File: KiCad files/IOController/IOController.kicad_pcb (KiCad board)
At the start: 2 copper layers, 22.5 x 48.5 mm, 13 parts, among them J1 AVR-ISP-6, J2 XT60 Horizontal Male, J3 XT60 Horizontal Socket, J4 Conn_01x02, J5 Conn_01x02, SW1 RotaryEncoder_Switch, SW2 SW_Push, U1 ATtiny85-20P, U3 LP2985-1.8

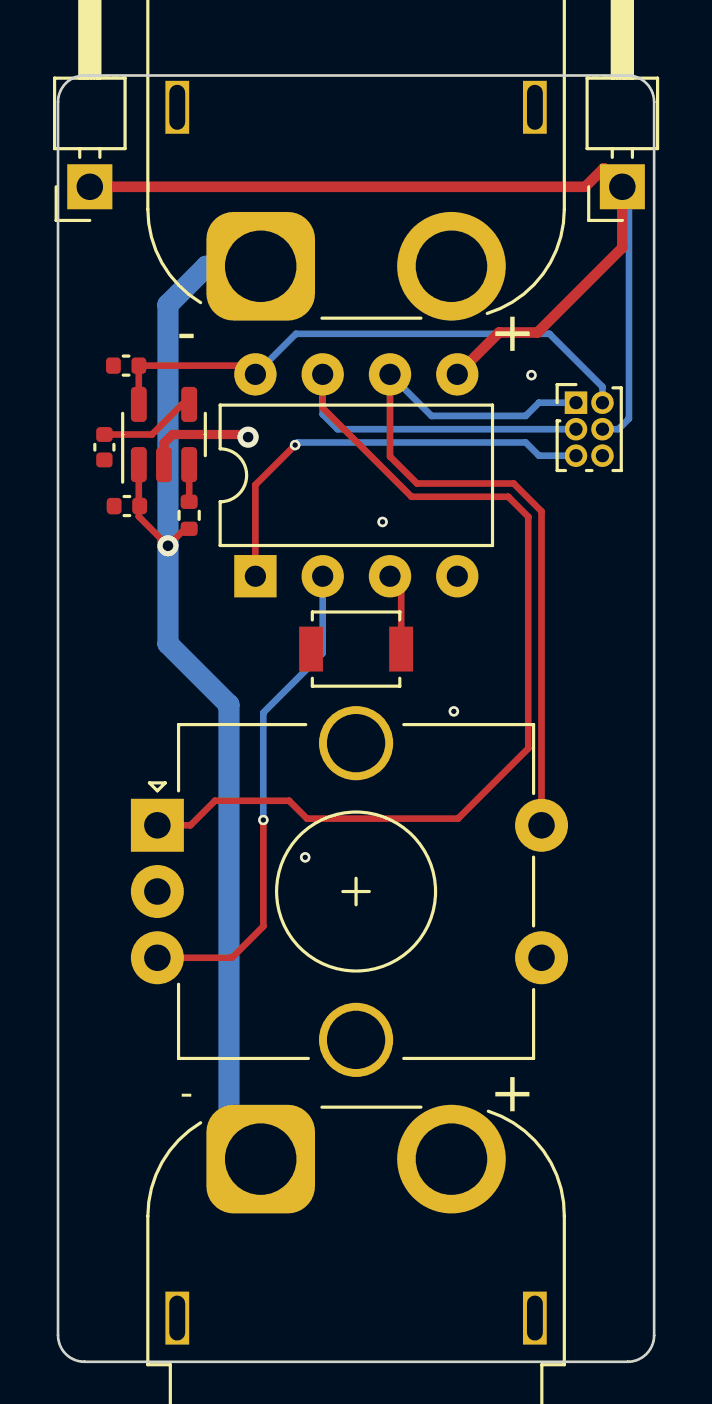
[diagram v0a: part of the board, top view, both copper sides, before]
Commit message: corrected VCC and GND being swapped
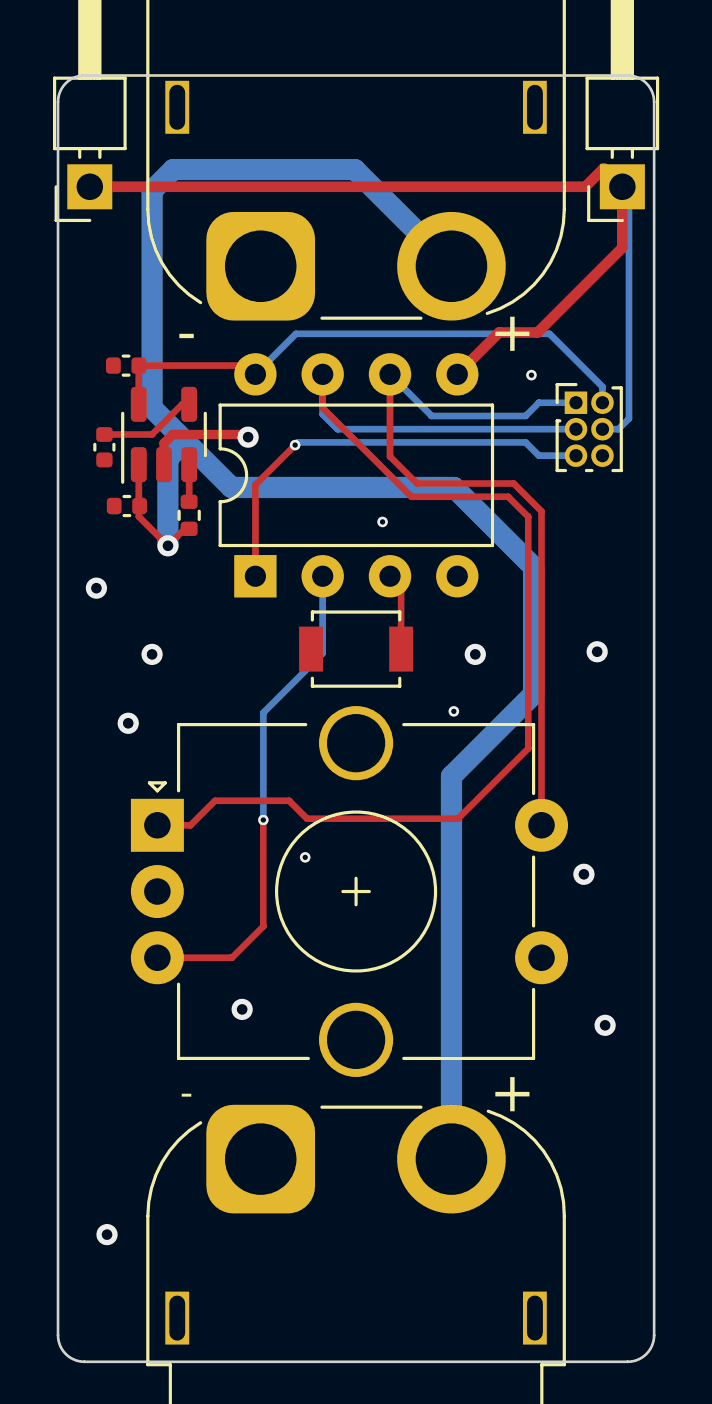
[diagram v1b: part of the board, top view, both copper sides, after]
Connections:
- J2 pad 1: VCC -> GND
- J2 pad 2: GND -> VCC
- J3 pad 1: VCC -> GND
- J3 pad 2: GND -> VCC
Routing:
- net VCC: track 42.4 -> 70.7 mm
- net GND: vias 5 -> 14
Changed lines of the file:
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@@
     (pad "" thru_hole rect locked (at 3.15 -6 180) (size 0.9 2) (drill oval 0.6 1.7) (layers "*.Cu" "*.Mask"))
     (pad "1" thru_hole roundrect locked (at 0 0 180) (size 4.1 4.1) (drill 2.7) (layers "*.Cu" "*.Mask") (roundrect_rratio 0.25)
-      (net 1 "VCC") (pinfunction "Pin_1") (pintype "passive"))
+      (net 2 "GND") (pinfunction "Pin_1") (pintype "passive"))
     (pad "2" thru_hole circle locked (at -7.2 0 180) (size 4.1 4.1) (drill 2.7) (layers "*.Cu" "*.Mask")
-      (net 2 "GND") (pinfunction "Pin_2") (pintype "passive"))
+      (net 1 "VCC") (pinfunction "Pin_2") (pintype "passive"))
     (model "${KIPRJMOD}/libraries/XT60PW FEMALE.STEP"
       (offset (xyz -3.6 15.15 4.5))
@@
     (pad "" thru_hole rect locked (at 10.35 -6) (size 0.9 2) (drill oval 0.6 1.7) (layers "*.Cu" "*.Mask"))
     (pad "1" thru_hole roundrect locked (at 0 0) (size 4.1 4.1) (drill 2.7) (layers "*.Cu" "*.Mask") (roundrect_rratio 0.25)
-      (net 1 "VCC") (pinfunction "Pin_1") (pintype "passive"))
+      (net 2 "GND") (pinfunction "Pin_1") (pintype "passive"))
     (pad "2" thru_hole circle locked (at 7.2 0) (size 4.1 4.1) (drill 2.7) (layers "*.Cu" "*.Mask")
-      (net 2 "GND") (pinfunction "Pin_2") (pintype "passive"))
+      (net 1 "VCC") (pinfunction "Pin_2") (pintype "passive"))
     (model "${KICAD6_3DMODEL_DIR}/Connector_AMASS.3dshapes/AMASS_XT60PW-M_1x02_P7.20mm_Horizontal.wrl"
       (offset (xyz 0 0 0))
@@
   (segment (start 24.3 49.1) (end 24.3 47.1375) (width 0.25) (layer "F.Cu") (net 1))
   (via (at 25.4 50.2) (size 0.8) (drill 0.4) (layers "F.Cu" "B.Cu") (net 1))
-  (segment (start 26.85 39.65) (end 25.4 41.1) (width 0.8) (layer "B.Cu") (net 1))
-  (segment (start 27.7 56.2) (end 27.7 72.15) (width 0.8) (layer "B.Cu") (net 1))
-  (segment (start 25.4 41.1) (end 25.4 53.9) (width 0.8) (layer "B.Cu") (net 1))
-  (segment (start 28.9 39.65) (end 26.85 39.65) (width 0.8) (layer "B.Cu") (net 1))
-  (segment (start 25.4 53.9) (end 27.7 56.2) (width 0.8) (layer "B.Cu") (net 1))
-  (segment (start 27.7 72.15) (end 28.9 73.35) (width 0.8) (layer "B.Cu") (net 1))
+  (segment (start 36.1 58.9) (end 39.2 55.8) (width 0.8) (layer "B.Cu") (net 1))
+  (segment (start 27.8 48) (end 26.05 46.25) (width 0.8) (layer "B.Cu") (net 1))
+  (segment (start 25.6 36) (end 32.45 36) (width 0.8) (layer "B.Cu") (net 1))
+  (segment (start 25.4 46.9) (end 26.05 46.25) (width 0.8) (layer "B.Cu") (net 1))
+  (segment (start 36.1 73.35) (end 36.1 58.9) (width 0.8) (layer "B.Cu") (net 1))
+  (segment (start 24.8 45) (end 24.8 36.8) (width 0.8) (layer "B.Cu") (net 1))
+  (segment (start 39.2 51) (end 36.2 48) (width 0.8) (layer "B.Cu") (net 1))
+  (segment (start 39.2 55.8) (end 39.2 51) (width 0.8) (layer "B.Cu") (net 1))
+  (segment (start 25.4 50.2) (end 25.4 46.9) (width 0.8) (layer "B.Cu") (net 1))
+  (segment (start 24.8 36.8) (end 25.6 36) (width 0.8) (layer "B.Cu") (net 1))
+  (segment (start 26.05 46.25) (end 24.8 45) (width 0.8) (layer "B.Cu") (net 1))
+  (segment (start 36.2 48) (end 27.8 48) (width 0.8) (layer "B.Cu") (net 1))
+  (segment (start 32.45 36) (end 36.1 39.65) (width 0.8) (layer "B.Cu") (net 1))
   (segment (start 28.325 46) (end 28.425 46.1) (width 0.35) (layer "F.Cu") (net 2))
   (segment (start 25.25 47.1375) (end 25.25 46.325) (width 0.35) (layer "F.Cu") (net 2))
   (segment (start 25.25 46.325) (end 25.575 46) (width 0.35) (layer "F.Cu") (net 2))
   (segment (start 25.575 46) (end 28.325 46) (width 0.35) (layer "F.Cu") (net 2))
+  (via (at 23.1 76.2) (size 0.8) (drill 0.4) (layers "F.Cu" "B.Cu") (free) (net 2))
   (via (at 28.425 46.1) (size 0.8) (drill 0.4) (layers "F.Cu" "B.Cu") (net 2))
+  (via (at 22.7 51.8) (size 0.8) (drill 0.4) (layers "F.Cu" "B.Cu") (free) (net 2))
   (via (at 39.12 43.76) (size 0.4) (drill 0.2) (layers "F.Cu" "B.Cu") (free) (net 2))
+  (via (at 41.9 68.3) (size 0.8) (drill 0.4) (layers "F.Cu" "B.Cu") (free) (net 2))
+  (via (at 37 54.3) (size 0.8) (drill 0.4) (layers "F.Cu" "B.Cu") (free) (net 2))
+  (via (at 24.8 54.3) (size 0.8) (drill 0.4) (layers "F.Cu" "B.Cu") (free) (net 2))
+  (via (at 23.9 56.9) (size 0.8) (drill 0.4) (layers "F.Cu" "B.Cu") (free) (net 2))
+  (via (at 28.2 67.7) (size 0.8) (drill 0.4) (layers "F.Cu" "B.Cu") (free) (net 2))
   (via (at 30.58 61.96) (size 0.4) (drill 0.2) (layers "F.Cu" "B.Cu") (free) (net 2))
   (via (at 36.19 56.45) (size 0.4) (drill 0.2) (layers "F.Cu" "B.Cu") (free) (net 2))
+  (via (at 41.1 62.6) (size 0.8) (drill 0.4) (layers "F.Cu" "B.Cu") (free) (net 2))
+  (via (at 41.6 54.2) (size 0.8) (drill 0.4) (layers "F.Cu" "B.Cu") (free) (net 2))
   (via (at 33.5 49.3) (size 0.4) (drill 0.2) (layers "F.Cu" "B.Cu") (net 2))
   (segment (start 30.65 60.5) (end 36.35 60.5) (width 0.25) (layer "F.Cu") (net 3))

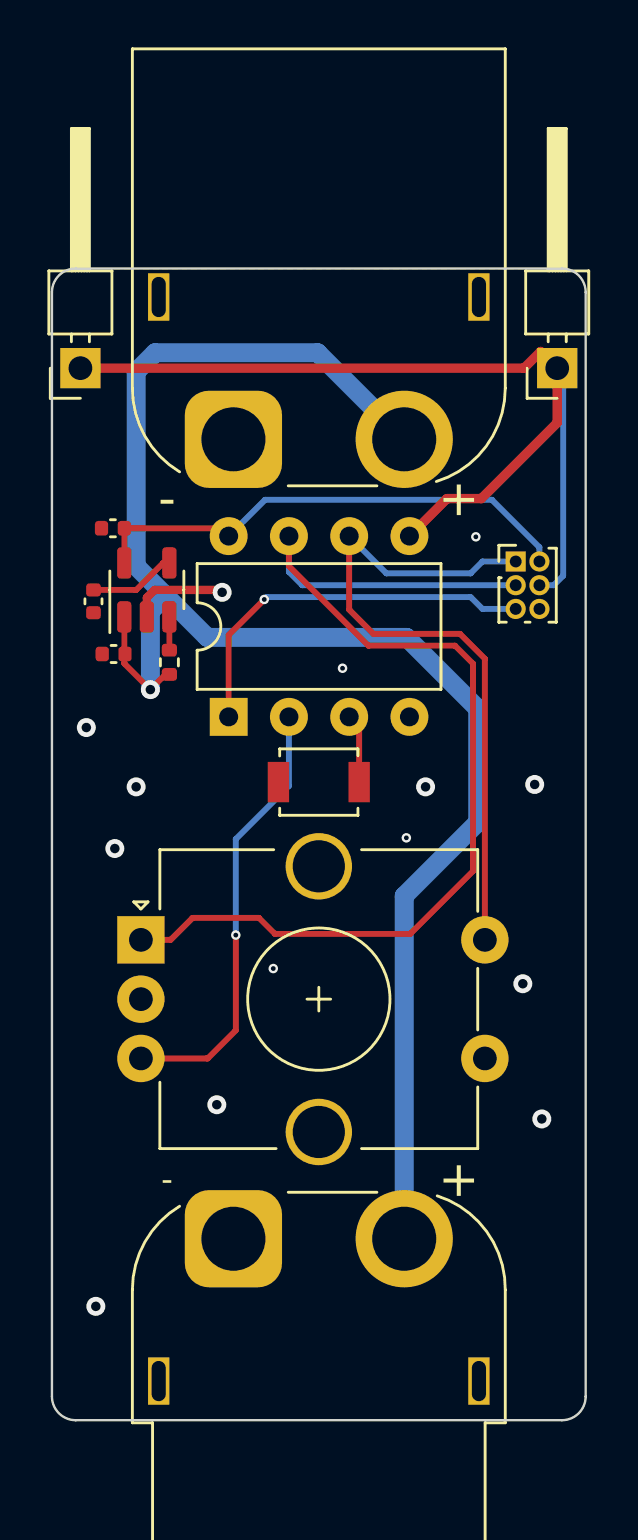
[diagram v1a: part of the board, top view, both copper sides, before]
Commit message: changed an XT60 to edge connector because I didnt like the XT60 and pin header setup.
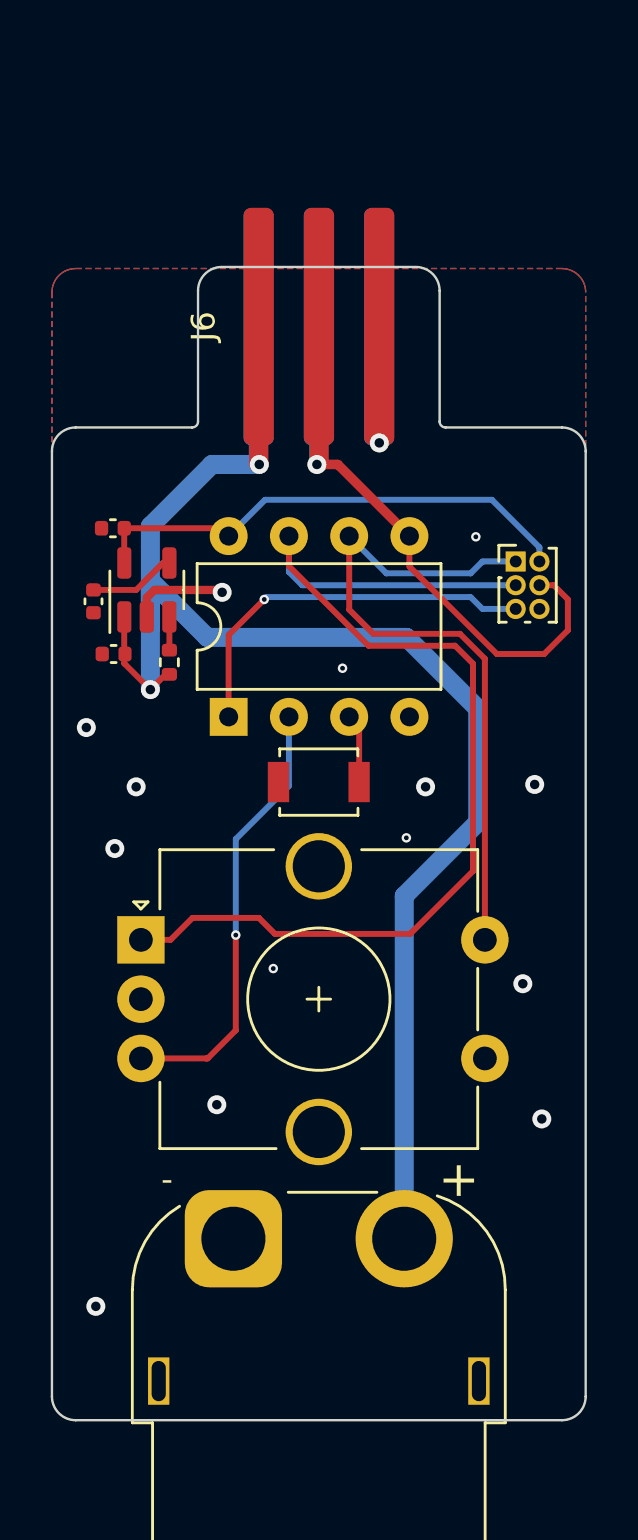
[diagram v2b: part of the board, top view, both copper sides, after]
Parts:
- removed J2: XT60 Horizontal Male, Connector_AMASS:AMASS_XT60PW-M_1x02_P7.20mm_Horizontal
- removed J4, J5: Conn_01x02, Connector_PinHeader_2.54mm:PinHeader_1x01_P2.54mm_Horizontal
- added J6: XT60 Horizontal Socket, Connector_PinHeader_2.54mm:PinHeader_1x03_P2.54mm_Vertical, F.Cu at (30.0, 34.9)
- added J6: XT60 Horizontal Socket, Connector_PinHeader_2.54mm:PinHeader_1x03_P2.54mm_Vertical, B.Cu at (30.0, 34.9)
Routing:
- net NPN-Gate: track 41.2 -> 29.5 mm, vias 0 -> 1
- net GND: track 4.16 -> 14.0 mm, vias 14 -> 15
- net VCC: track 70.7 -> 70.5 mm, vias 1 -> 2
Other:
- board size 22.5 x 48.5 mm -> 22.5 x 48.6 mm

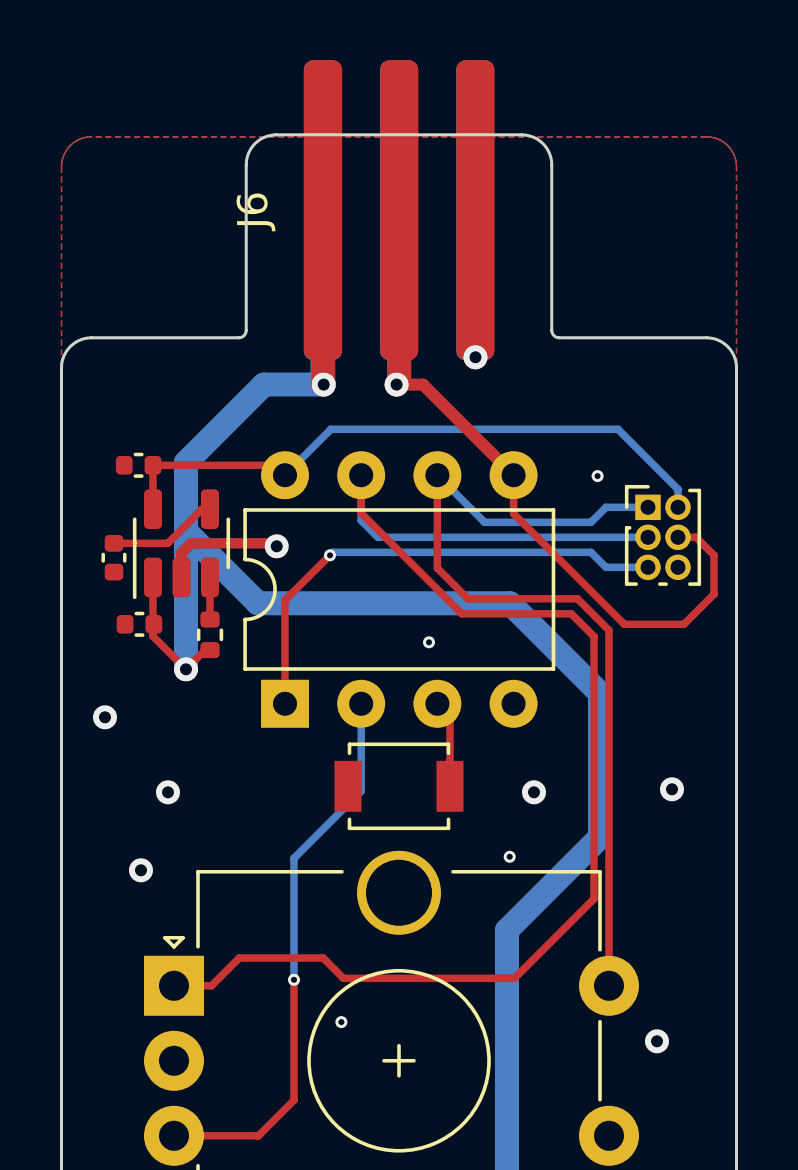
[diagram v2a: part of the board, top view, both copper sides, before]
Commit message: added footprints for some discontinued LEDs i have spare of, added level shifter to ensure gate voltage is above threshold
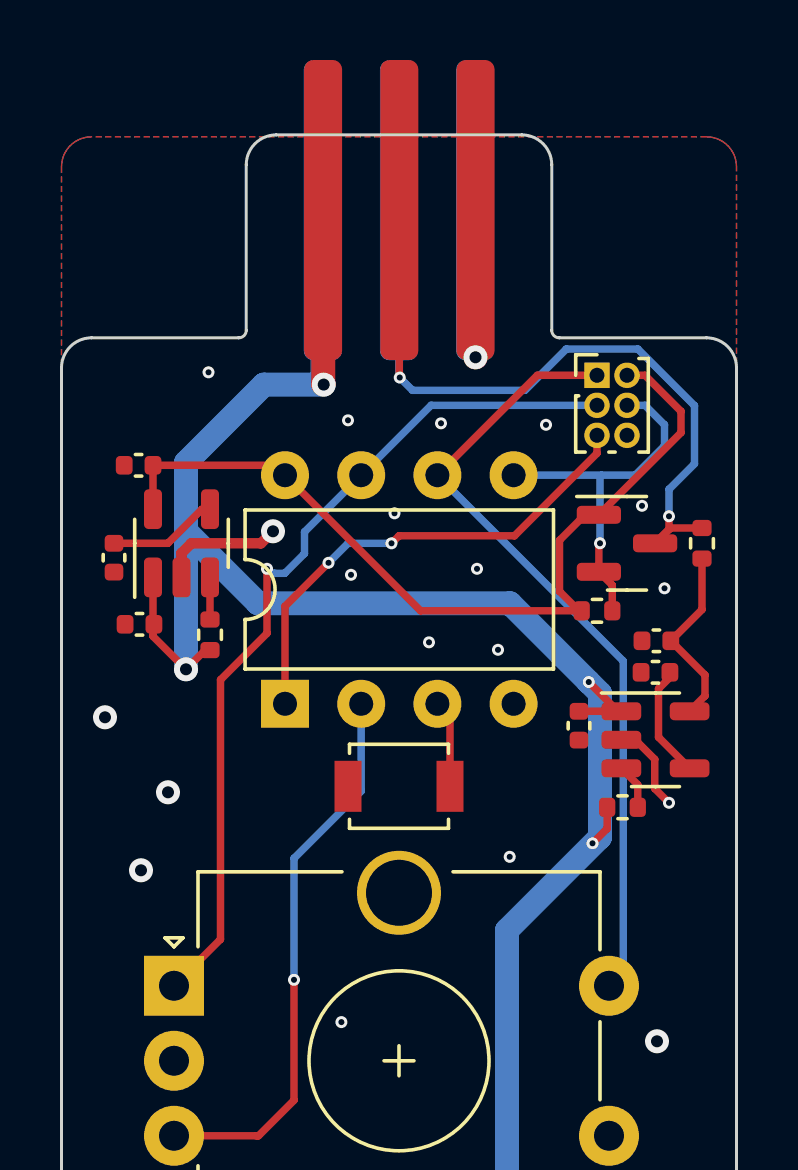
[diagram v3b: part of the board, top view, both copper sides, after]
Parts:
- added C4: 0402 1uF, Capacitor_SMD:C_0402_1005Metric, F.Cu at (38.5, 52.1)
- added C5: 0402 10nF, Capacitor_SMD:C_0402_1005Metric, F.Cu at (41.0, 50.3)
- added C6: 0402 2.2uF, Capacitor_SMD:C_0402_1005Metric, F.Cu at (41.1, 49.2)
- added Q1: BSS138, Package_TO_SOT_SMD:SOT-23, F.Cu at (40.1, 46.0)
- added R2: 10K 0402, Resistor_SMD:R_0402_1005Metric, F.Cu at (40.0, 54.8)
- added R3: 10K 0402, Resistor_SMD:R_0402_1005Metric, F.Cu at (39.1, 48.2)
- added R4: 10K 0402, Resistor_SMD:R_0402_1005Metric, F.Cu at (42.6, 46.0)
- added U4: LP2985-5.0, Package_TO_SOT_SMD:SOT-23-5, F.Cu at (41.0, 52.5)
- moved J1 4.72 mm to (39.1, 40.4)
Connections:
- net VDD renamed +1V8
- J1 pad 4: NPN-Gate -> NPN-Gate_1.8V
- J6 pad 2: NPN-Gate -> NPN-Gate_5V (x2)
- U1 pad 5: NPN-Gate -> NPN-Gate_1.8V
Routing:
- net NPN-Gate: track 29.5 -> 0.00 mm, vias 1 -> 0
- net NPN-Gate_5V: track 0.00 -> 29.4 mm, vias 0 -> 2
- net ROT_A: track 46.5 -> 29.0 mm, vias 0 -> 1
- net NPN-Gate_1.8V: track 0.00 -> 12.4 mm, vias 0 -> 1
- net +1V8: track 21.2 -> 29.0 mm
- net +5V: track 0.00 -> 6.21 mm
- net VCC: track 70.5 -> 74.8 mm, vias 2 -> 4
- net Net-(U4-BP): track 0.00 -> 3.79 mm
- net GND: track 14.0 -> 17.0 mm, vias 15 -> 23
- net ROT_SW1: track 29.4 -> 26.5 mm
- net Net-(U4-ON/~{OFF}): track 0.00 -> 1.53 mm
- net Net-(J1-~{RST}): vias 1 -> 2

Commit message: some partial work towards modifying the design yet again
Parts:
- added C10: 22uF, Capacitor_SMD:C_0805_2012Metric, F.Cu at (56.7, 56.7)
- added C11: 100nF, Capacitor_SMD:C_0805_2012Metric, F.Cu at (56.7, 59.7)
- added C7: 10uF 0805, Capacitor_SMD:C_0805_2012Metric, F.Cu at (56.7, 47.6)
- added C8: 100nF 0805, Capacitor_SMD:C_0805_2012Metric, F.Cu at (56.7, 50.6)
- added C9: 100nF, Capacitor_SMD:C_0805_2012Metric, F.Cu at (56.7, 53.6)
- added L1: MDA7030-2R2M, Inductor_SMD:L_Coilcraft_XAL7030-222, F.Cu at (32.5, 47.0)
- added PS1: TPS566242DRLR, Package_TO_SOT_SMD:SOT-563, F.Cu at (32.5, 53.5)
- added R5: 100K 0805, Resistor_SMD:R_0805_2012Metric, F.Cu at (61.2, 47.6)
- added R6: 23.2K 0805, Resistor_SMD:R_0805_2012Metric, F.Cu at (61.2, 50.5)
- added R7: 120K 0805, Resistor_SMD:R_0805_2012Metric, F.Cu at (61.2, 53.5)
- added R8: 30K 0805, Resistor_SMD:R_0805_2012Metric, F.Cu at (61.2, 56.4)
- moved J3 20.0 mm to (28.9, 93.3)
- moved SW1 18.8 mm to (25.0, 79.5)
- moved C2 18.0 mm to (23.0, 64.4)
- moved C1 18.0 mm to (23.9, 66.7)
- moved C3 18.0 mm to (23.8, 61.4)
- moved C4 18.0 mm to (38.5, 70.0)
- moved C5 18.0 mm to (41.0, 68.2)
- moved C6 18.0 mm to (41.1, 67.2)
- moved J1 18.0 mm to (39.1, 58.4)
- moved Q1 18.0 mm to (40.1, 64.0)
- moved R1 18.0 mm to (26.2, 67.0)
- moved R2 18.0 mm to (40.0, 72.8)
- moved R3 18.0 mm to (39.1, 66.2)
- moved R4 18.0 mm to (42.6, 64.0)
- moved U3 18.0 mm to (25.2, 64.0)
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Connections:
- J6 pad 1: VCC -> VDD (x2)
- J6 pad 2: NPN-Gate_5V -> unconnected-(J6-Pin_2-Pad2) (x2)
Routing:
- net VCC: track 74.8 -> 0.00 mm, vias 4 -> 0
- net NPN-Gate_5V: track 29.4 -> 0.00 mm, vias 2 -> 0
- net +1V8: track 29.0 -> 0.00 mm
- net ROT_A: track 29.0 -> 0.00 mm, vias 1 -> 0
- net ROT_SW1: track 26.5 -> 0.00 mm
- net ROT_B: track 18.6 -> 0.00 mm, vias 1 -> 0
- net GND: track 17.0 -> 0.00 mm, vias 23 -> 0
- net Net-(J1-~{RST}): track 16.4 -> 0.00 mm, vias 2 -> 0
- net NPN-Gate_1.8V: track 12.4 -> 0.00 mm, vias 1 -> 0
- net +5V: track 6.21 -> 0.00 mm
- net Net-(U4-BP): track 3.79 -> 0.00 mm
- net Net-(U3-BP): track 3.67 -> 0.00 mm
- net SW1: track 2.92 -> 0.00 mm
- net Net-(U4-ON/~{OFF}): track 1.53 -> 0.00 mm
- net Net-(U3-ON/~{OFF}): track 1.40 -> 0.00 mm
- removed copper zone on B.Cu, net GND
- removed copper zone on F.Cu, net GND
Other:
- board size 22.5 x 48.6 mm -> 22.5 x 68.6 mm
